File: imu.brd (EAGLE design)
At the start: 160 x 100 mm, 51 parts, among them IC1 TM4C123[6,F]XXPM, IC2 FT230XQ, U1 MPU-6000QFN-24, U2 ADXL345

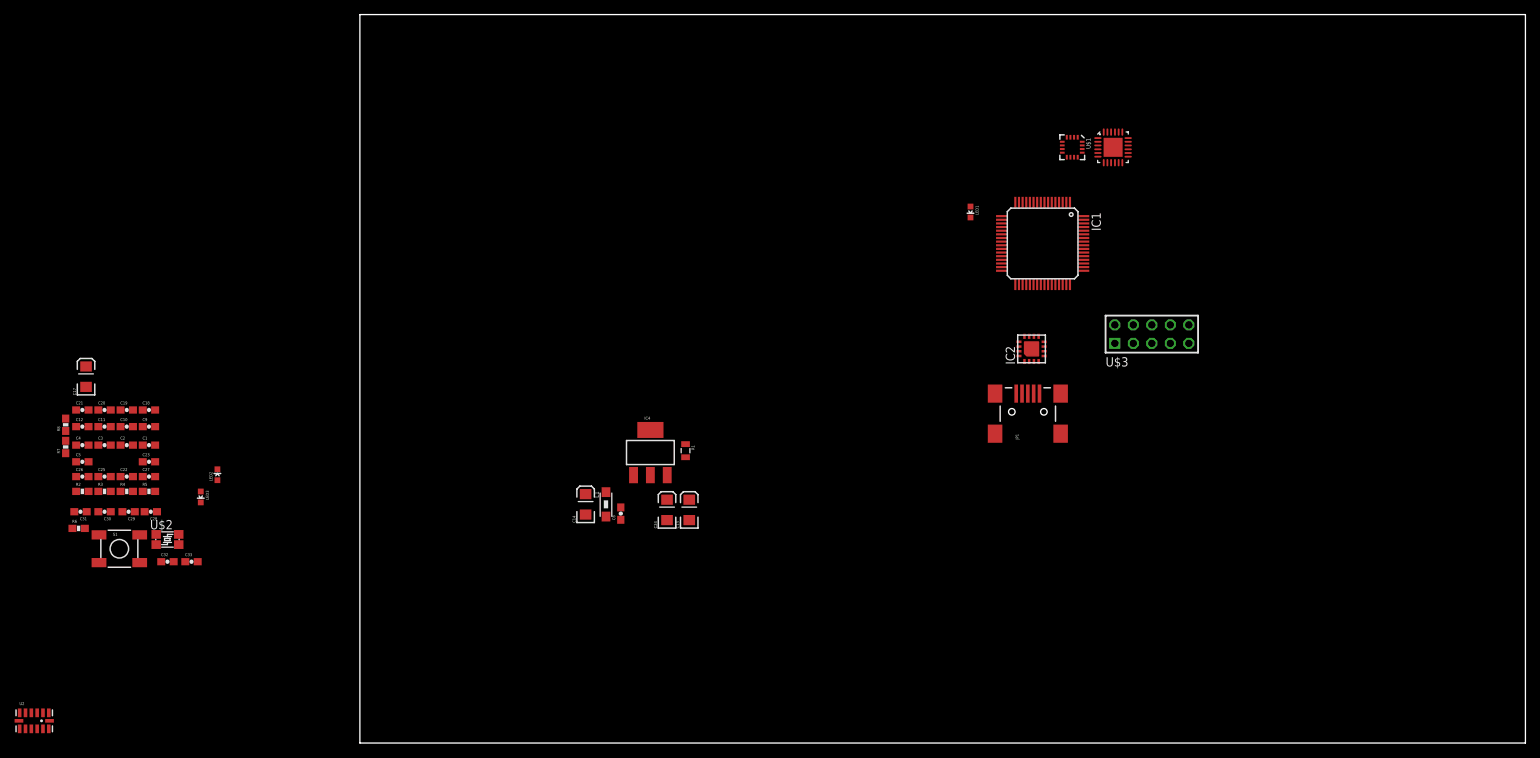
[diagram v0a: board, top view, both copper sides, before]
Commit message: Modification to schematics and board
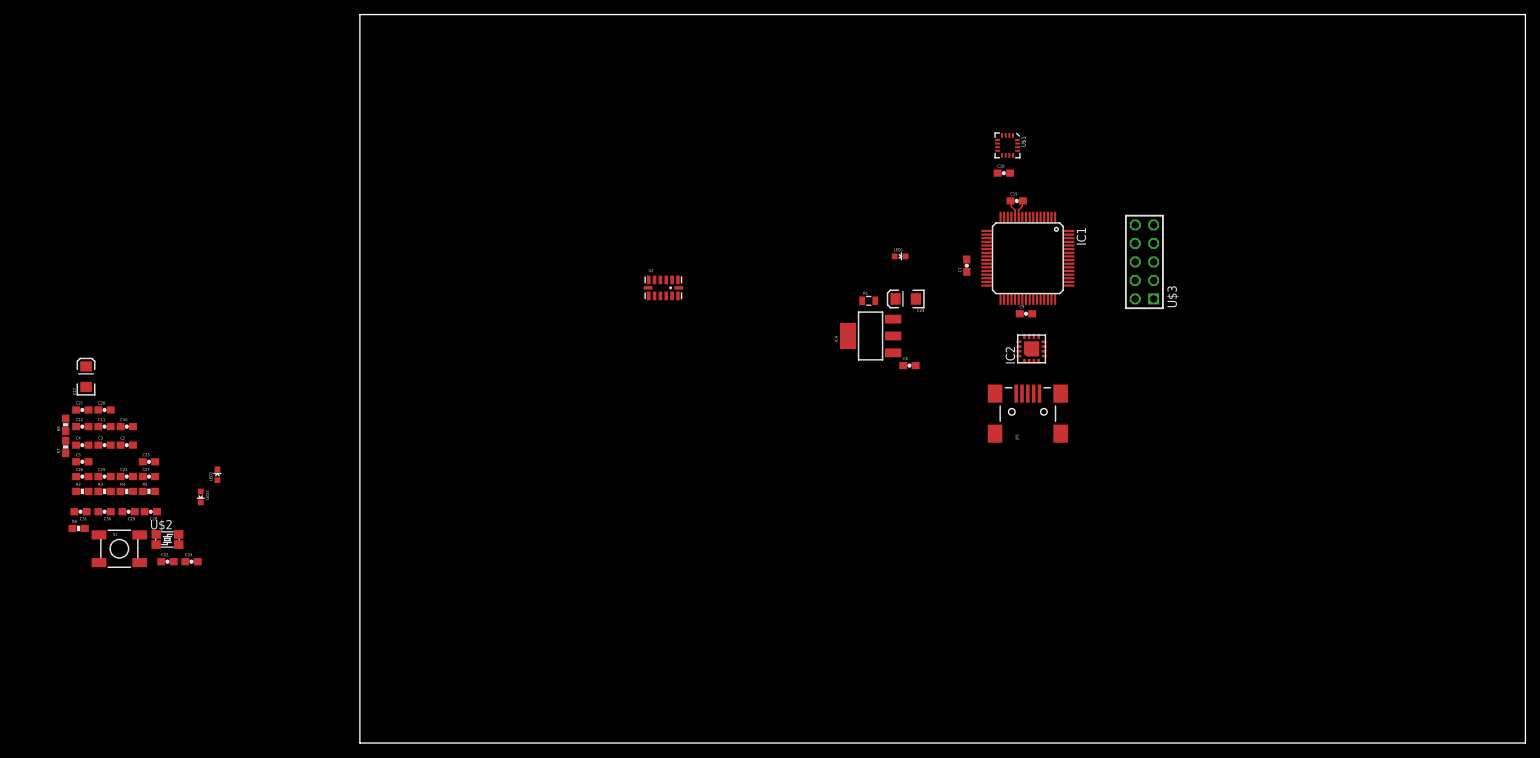
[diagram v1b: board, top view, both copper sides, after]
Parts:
- removed C13: 10uF, SparkFun-Capacitors:EIA3216
- removed C14: 4.7uF, SparkFun-Capacitors:EIA3216
- removed L1: 10uH, Wuerth_Elektronik_eiSos_V6:1206
- removed U1: MPU-6000QFN-24, SparkFun-Sensors:QFN-24-TESTING
- moved C19 125.5 mm to (90.2, 74.4)
- moved C18 121.8 mm to (88.4, 78.2)
- moved C9 121.4 mm to (91.4, 58.9)
- moved C1 114.9 mm to (83.3, 65.5), turned to 90 degrees
- moved U2 104.8 mm to (41.7, 62.5)
- moved C6 44.5 mm to (75.4, 51.8), turned to 0 degrees
- moved C24 43.7 mm to (74.9, 61.0), turned to 180 degrees
- moved IC4 34.2 mm to (70.1, 55.9), turned to 90 degrees
- moved R1 32.5 mm to (69.8, 60.7), turned to 0 degrees
- moved LED1 11.4 mm to (74.2, 66.8), turned to 270 degrees
- moved U$3 9.96 mm to (107.7, 66.0), turned to 90 degrees
- moved U$1 8.89 mm to (88.9, 82.0)
- moved IC1 2.87 mm to (91.7, 66.5)
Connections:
- removed net N$3: C10.2, C14.A, C9.2, IC4.3, L1.2
- net 5V: now also C10.2, C9.2, IC4.3; no longer C13.A, L1.1
- net GND: no longer C13.C, C14.C
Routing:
- net GND: track 0.00 -> 2.53 mm
- net 3.3V: track 0.00 -> 2.51 mm
